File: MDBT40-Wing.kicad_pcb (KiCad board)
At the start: 2 copper layers, 21.3 x 27.4 mm, 3 parts, among them J1 Left, J2 Right, U1 MDBT40

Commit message: Final touches
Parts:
- added G***: LOGO, ktec_logo:ktec_logo, B.Cu at (147.2, 108.3)
- moved U1 175.4 mm to (144.8, 99.1)
- moved J1 175.4 mm to (135.9, 88.9)
- moved J2 175.4 mm to (153.7, 88.9)
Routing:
- net /39: track 11.9 -> 10.6 mm
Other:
- board text added: "AVDD"
- board text added: "DCC"
- board text added: "DEC2"
- board text added: "Designed by K.T.E.C. https://ktec.io"
- board text added: "GND"
- board text added: "P0.00"
- board text added: "P0.01"
- board text added: "P0.02"
- board text added: "P0.03"
- board text added: "P0.04"
- board text added: "P0.05"
- board text added: "P0.06"
- board text added: "P0.07"
- board text added: "P0.08"
- board text added: "P0.09"
- board text added: "P0.10"
- board text added: "P0.11"
- board text added: "P0.12"
- board text added: "P0.13"
- board text added: "P0.14"
- board text added: "P0.15"
- board text added: "P0.16"
- board text added: "P0.17"
- board text added: "P0.18"
- board text added: "P0.19"
- board text added: "P0.20"
- board text added: "P0.21"
- board text added: "P0.22"
- board text added: "P0.23"
- board text added: "P0.24"
- board text added: "P0.25"
- board text added: "P0.26"
- board text added: "P0.27"
- board text added: "P0.28"
- board text added: "P0.29"
- board text added: "P0.30"
- board text added: "SWCLK"
- board text added: "SWDIO"
- board text added: "VDD"

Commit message: update design
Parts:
- removed G***: LOGO, ktec_logo:ktec_logo
- removed J1: Left, Pin_Headers:Pin_Header_Straight_1x21_Pitch1.27mm
- removed J2: Right, Pin_Headers:Pin_Header_Straight_1x21_Pitch1.27mm
- removed U1: MDBT40, mdbt40_carrier:MDBT40-Carrier
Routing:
- net /21: track 15.9 -> 0.00 mm
- net /5: track 15.8 -> 0.00 mm, vias 1 -> 0
- net /20: track 14.6 -> 0.00 mm
- net /6: track 14.5 -> 0.00 mm, vias 1 -> 0
- net /19: track 13.8 -> 0.00 mm
- net /4: track 13.8 -> 0.00 mm, vias 2 -> 0
- net /18: track 13.1 -> 0.00 mm
- net /22: track 12.3 -> 0.00 mm
- net /17: track 12.3 -> 0.00 mm
- net /16: track 11.2 -> 0.00 mm
- net /3: track 11.1 -> 0.00 mm
- net /38: track 11.0 -> 0.00 mm, vias 1 -> 0
- net /23: track 10.9 -> 0.00 mm
- net /39: track 10.6 -> 0.00 mm, vias 1 -> 0
- net /11: track 10.1 -> 0.00 mm, vias 1 -> 0
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- removed copper zone on B.Cu, net (none)
- removed copper zone on F.Cu, net (none)
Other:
- board outline removed

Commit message: Design #6
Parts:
- added J1: LEFT, Pin_Headers:Pin_Header_Straight_1x14_Pitch2.54mm, F.Cu at (-9.65, -4.06)
- added J2: RIGHT, Pin_Headers:Pin_Header_Straight_1x14_Pitch2.54mm, F.Cu at (13.2, -4.06)
- added J3: BOTTOM, Pin_Headers:Pin_Header_Straight_1x08_Pitch2.54mm, F.Cu at (-7.11, 29.0)
- added J4: DCC, sing_pad:1Pin, B.Cu at (-4.57, 23.9)
- added J5: DEC2, sing_pad:1Pin, B.Cu at (8.64, 23.9)
- added JP1: Jumper, Connectors:GS2, B.Cu at (-4.57, 15.7)
- added U1: MDBT40, mdbt40_carrier:MDBT40-Carrier, F.Cu at (2.03, 3.56)
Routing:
- net /GND: track 0.00 -> 57.1 mm, vias 0 -> 3
- net /SWCLK: track 0.00 -> 33.6 mm, vias 0 -> 1
- net /SWDIO: track 0.00 -> 30.9 mm, vias 0 -> 1
- net /DEC2: track 0.00 -> 27.5 mm, vias 0 -> 1
- net /AVDD: track 0.00 -> 23.3 mm, vias 0 -> 1
- net /P0.00: track 0.00 -> 20.9 mm
- net /P0.01: track 0.00 -> 20.1 mm
- net /VDD: track 0.00 -> 19.3 mm, vias 0 -> 1
- net /P0.07: track 0.00 -> 19.2 mm
- net /P0.08: track 0.00 -> 19.0 mm
- net /P0.10: track 0.00 -> 18.6 mm
- net /P0.02: track 0.00 -> 18.5 mm
- net /P0.06: track 0.00 -> 18.2 mm
- net /P0.09: track 0.00 -> 18.1 mm
- net /P0.03: track 0.00 -> 17.7 mm
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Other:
- board outline added: 25.9 x 36.6 mm
- board text removed: "AVDD"
- board text removed: "DCC"
- board text removed: "DEC2"
- board text removed: "Designed by K.T.E.C. https://ktec.io"
- board text removed: "GND"
- board text removed: "P0.00"
- board text removed: "P0.01"
- board text removed: "P0.02"
- board text removed: "P0.03"
- board text removed: "P0.04"
- board text removed: "P0.05"
- board text removed: "P0.06"
- board text removed: "P0.07"
- board text removed: "P0.08"
- board text removed: "P0.09"
- board text removed: "P0.10"
- board text removed: "P0.11"
- board text removed: "P0.12"
- board text removed: "P0.13"
- board text removed: "P0.14"
- board text removed: "P0.15"
- board text removed: "P0.16"
- board text removed: "P0.17"
- board text removed: "P0.18"
- board text removed: "P0.19"
- board text removed: "P0.20"
- board text removed: "P0.21"
- board text removed: "P0.22"
- board text removed: "P0.23"
- board text removed: "P0.24"
- board text removed: "P0.25"
- board text removed: "P0.26"
- board text removed: "P0.27"
- board text removed: "P0.28"
- board text removed: "P0.29"
- board text removed: "P0.30"
- board text removed: "SWCLK"
- board text removed: "SWDIO"
- board text removed: "VDD"

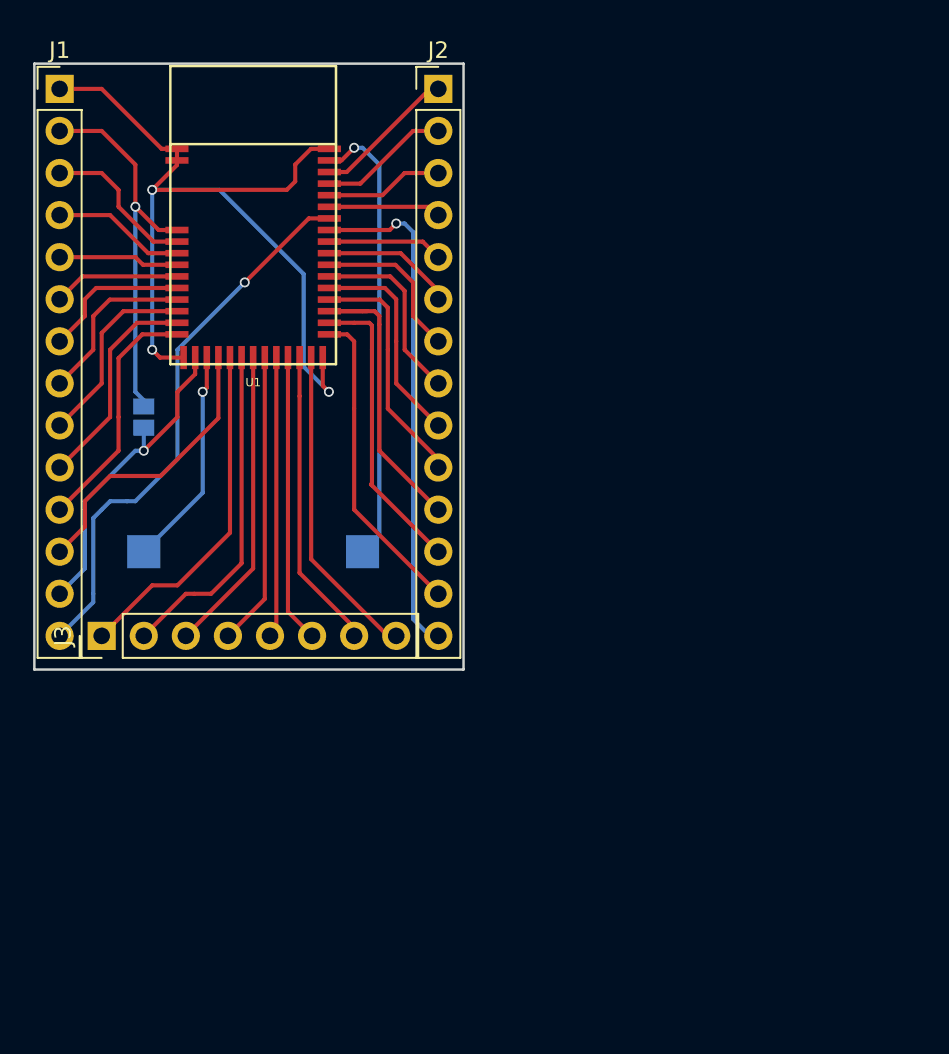
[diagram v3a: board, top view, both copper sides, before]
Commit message: Optimize edge and route
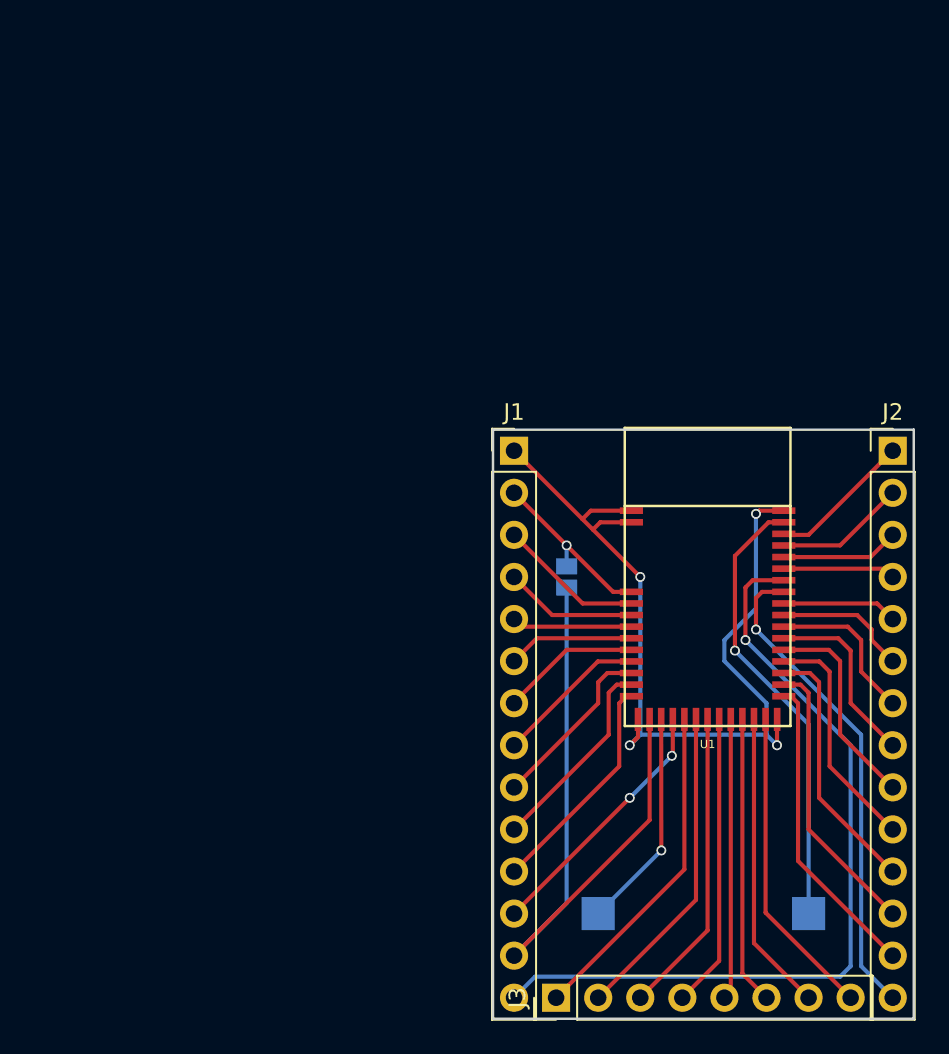
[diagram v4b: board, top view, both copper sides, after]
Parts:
- moved J1 35.1 mm to (17.8, 17.8)
- moved J2 35.1 mm to (40.6, 17.8)
- moved J3 35.1 mm to (20.3, 50.8)
- moved J4 35.1 mm to (22.9, 45.7)
- moved U1 35.1 mm to (29.5, 25.4)
- moved J5 34.7 mm to (35.6, 45.7)
- moved JP1 27.3 mm to (21.0, 25.4)
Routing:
- net /VDD: track 19.3 -> 41.2 mm, vias 1 -> 0
- net /SWCLK: track 33.6 -> 49.1 mm
- net /AVDD: track 23.3 -> 10.8 mm
- net /P0.10: track 18.6 -> 15.6 mm
- net /P0.30: track 17.5 -> 15.8 mm, vias 0 -> 2
- net /SWDIO: track 30.9 -> 29.4 mm
- net /P0.26: track 10.4 -> 9.18 mm
- net /P0.29: track 14.7 -> 13.7 mm
- net /P0.27: track 11.7 -> 10.7 mm
- net /GND: track 57.1 -> 56.1 mm, vias 3 -> 4
- net /P0.09: track 18.1 -> 17.1 mm
- net /P0.00: track 20.9 -> 20.0 mm
- net /P0.28: track 13.1 -> 12.2 mm
- net /P0.01: track 20.1 -> 19.2 mm
- net /P0.21: track 9.39 -> 8.80 mm
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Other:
- board size 25.9 x 36.6 mm -> 25.4 x 35.6 mm

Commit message: Design #7
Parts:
- J1, J2: footprint Pin_Headers:Pin_Header_Straight_1x14_Pitch2.54mm -> connectors:1X14
- J3: footprint Pin_Headers:Pin_Header_Straight_1x08_Pitch2.54mm -> connectors:2X4
- moved J3 12.2 mm to (32.4, 52.7), turned to 0 degrees
- moved J4 8.84 mm to (26.0, 54.0)
- moved J5 8.84 mm to (38.7, 54.0)
- moved JP1 4.49 mm to (24.1, 28.6)
- moved J1 4.49 mm to (21.0, 21.0), turned to 270 degrees
- moved J2 4.49 mm to (43.8, 21.0), turned to 270 degrees
- moved U1 4.31 mm to (32.4, 28.6)
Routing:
- net /GND: track 56.1 -> 8.52 mm, vias 4 -> 5
- net /SWCLK: track 49.1 -> 32.8 mm
- net /DEC2: track 27.2 -> 32.4 mm
- net /DCC: track 13.3 -> 18.3 mm
- net /P0.07: track 18.9 -> 14.4 mm
- net /P0.01: track 19.2 -> 15.5 mm
- net /P0.05: track 17.4 -> 14.6 mm
- net /P0.03: track 17.7 -> 15.1 mm
- net /P0.00: track 20.0 -> 18.9 mm
- net /P0.04: track 17.0 -> 17.9 mm
- net /P0.02: track 18.5 -> 17.7 mm
- net /P0.06: track 18.2 -> 17.4 mm
- added copper zone on B.Cu, net /GND
- added copper zone on F.Cu, net /GND
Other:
- net class Default: trace_width 0.25 -> 0.4064
- net class Power added: clearance 0.2, trace_width 0.6096, via_dia 0.6, via_drill 0.4
- board text added: "0"
- board text added: "1"
- board text added: "10"
- board text added: "11"
- board text added: "12"
- board text added: "13"
- board text added: "14"
- board text added: "15"
- board text added: "16"
- board text added: "17"
- board text added: "18"
- board text added: "19"
- board text added: "2"
- board text added: "20"
- board text added: "21"
- board text added: "22"
- board text added: "23"
- board text added: "24"
- board text added: "25"
- board text added: "26"
- board text added: "27"
- board text added: "28"
- board text added: "29"
- board text added: "3"
- board text added: "30"
- board text added: "4"
- board text added: "5"
- board text added: "6"
- board text added: "7"
- board text added: "8"
- board text added: "9"
- board text added: "AVDD"
- board text added: "DCC"
- board text added: "DEC2"
- board text added: "Designed by K.T.E.C."
- board text added: "GND"
- board text added: "MDBT40"
- board text added: "SWC"
- board text added: "SWD"
- board text added: "VDD"

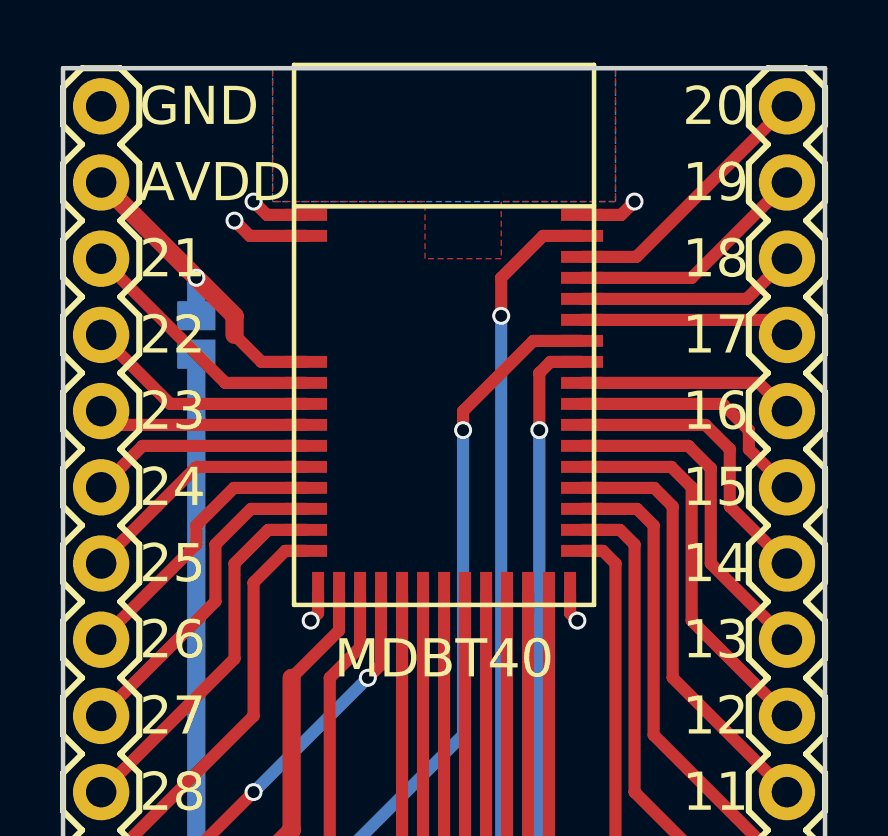
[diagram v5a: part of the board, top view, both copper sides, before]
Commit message: Use Adafruit's MDBT40 Mod
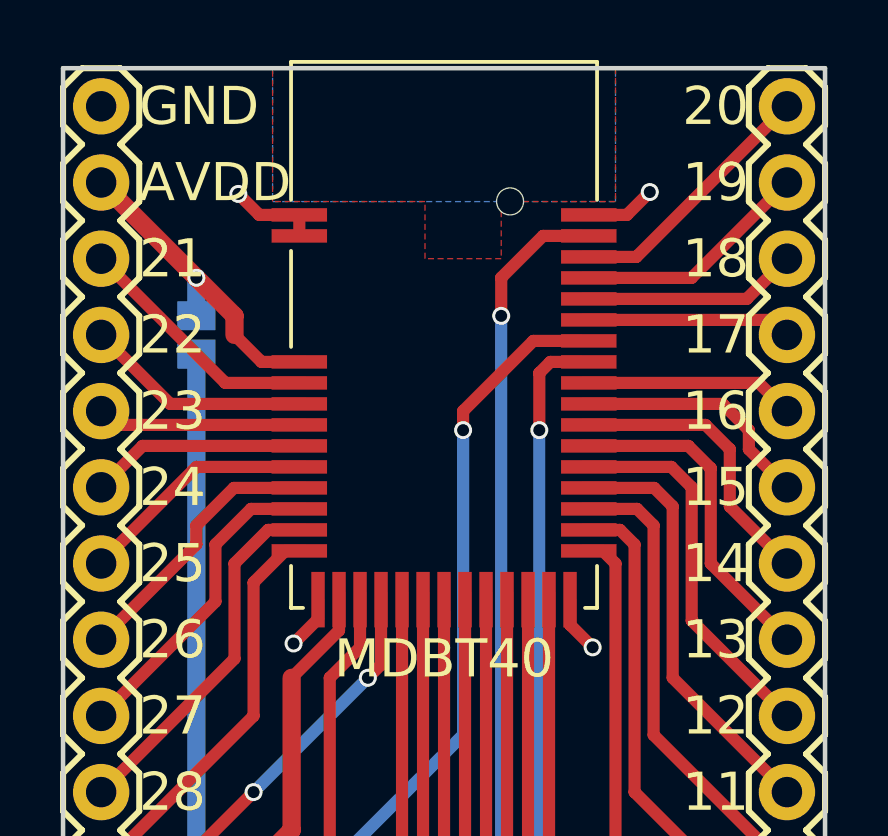
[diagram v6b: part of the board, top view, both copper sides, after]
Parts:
- U1: footprint mdbt40_carrier:MDBT40-Carrier -> mdbt40_carrier:ADA_MDBT40
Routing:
- net /GND: track 8.52 -> 9.07 mm, vias 5 -> 4

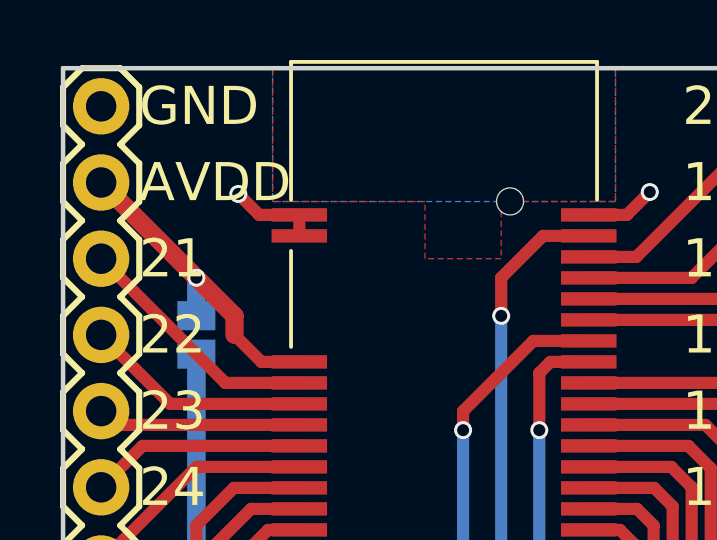
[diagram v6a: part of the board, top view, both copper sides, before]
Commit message: Minor change of trace of GND pins
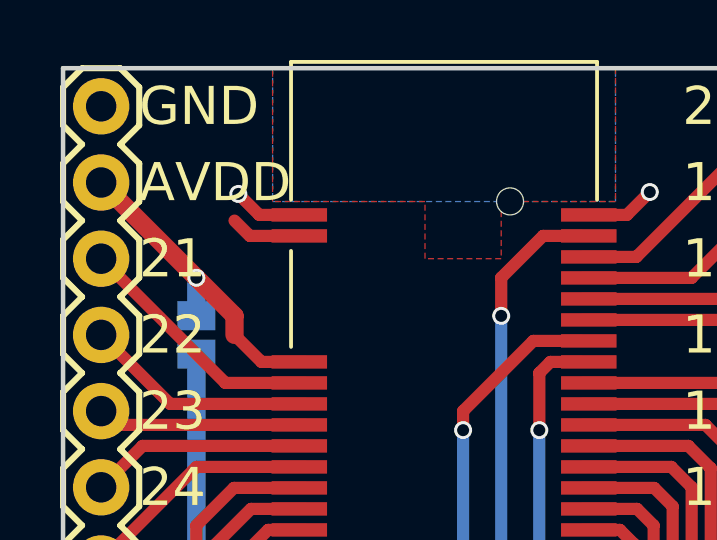
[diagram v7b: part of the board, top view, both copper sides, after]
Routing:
- net /GND: track 9.07 -> 10.7 mm
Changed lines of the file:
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@@
-(kicad_pcb (version 4) (host pcbnew 4.0.6)
+(kicad_pcb (version 4) (host pcbnew 4.0.2-stable)
   (general
     (links 44)
     (no_connects 0)
-    (area 19.609999 19.609999 45.160001 55.320001)
+    (area 10.109287 14.263486 54.660715 60.485001)
     (thickness 1.6)
     (drawings 58)
-    (tracks 153)
+    (tracks 154)
     (zones 0)
     (modules 7)
@@
   (gr_line (start 45.085 55.245) (end 19.685 55.245) (angle 90) (layer Edge.Cuts) (width 0.15))
   (gr_line (start 45.085 19.685) (end 45.085 55.245) (angle 90) (layer Edge.Cuts) (width 0.15))
+  (segment (start 27.56 25.275) (end 25.91 25.275) (width 0.4064) (layer F.Cu) (net 1) (status 400000))
+  (segment (start 25.91 25.275) (end 25.4 24.765) (width 0.4064) (layer F.Cu) (net 1))
   (segment (start 37.21 24.575) (end 38.4805 24.575) (width 0.4064) (layer F.Cu) (net 1))
   (via (at 39.243 23.8125) (size 0.6) (drill 0.4) (layers F.Cu B.Cu) (net 1))
@@
   (via (at 25.527 23.876) (size 0.6) (drill 0.4) (layers F.Cu B.Cu) (net 1))
   (segment (start 26.226 24.575) (end 25.527 23.876) (width 0.4064) (layer F.Cu) (net 1))
-  (segment (start 27.56 25.275) (end 27.56 24.575) (width 0.4064) (layer F.Cu) (net 1))
   (segment (start 36.585 37.4) (end 36.585 38.236) (width 0.4064) (layer F.Cu) (net 1))
   (segment (start 36.585 38.236) (end 37.338 38.989) (width 0.4064) (layer F.Cu) (net 1))
@@
       )
     )
+  )
+  (zone (net 0) (net_name "") (layer F.Cu) (hatch edge 0.508)
+    (connect_pads (clearance 0.508))
+    (min_thickness 0.254)
+    (keepout (tracks allowed) (vias allowed) (copperpour not_allowed))
+    (fill (arc_segments 16) (thermal_gap 0.508) (thermal_bridge_width 0.508))
+    (polygon
+      (pts
+        (xy 28.8925 25.7175) (xy 26.3525 25.7175) (xy 26.3525 24.13) (xy 28.8925 24.13) (xy 28.8925 25.7175)
+      )
+    )
